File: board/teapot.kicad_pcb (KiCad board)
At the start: 2 copper layers, 49.9 x 50 mm, 47 parts, among them J1 MICROUSB, P1 BATT, P2 SMA, Q1 TEPT4400, U1 TPS79333DBVR, U2 TLV61225, U4 RFM69W, U5 STM32L052K8, U6 HTU21D, U7 MS5637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

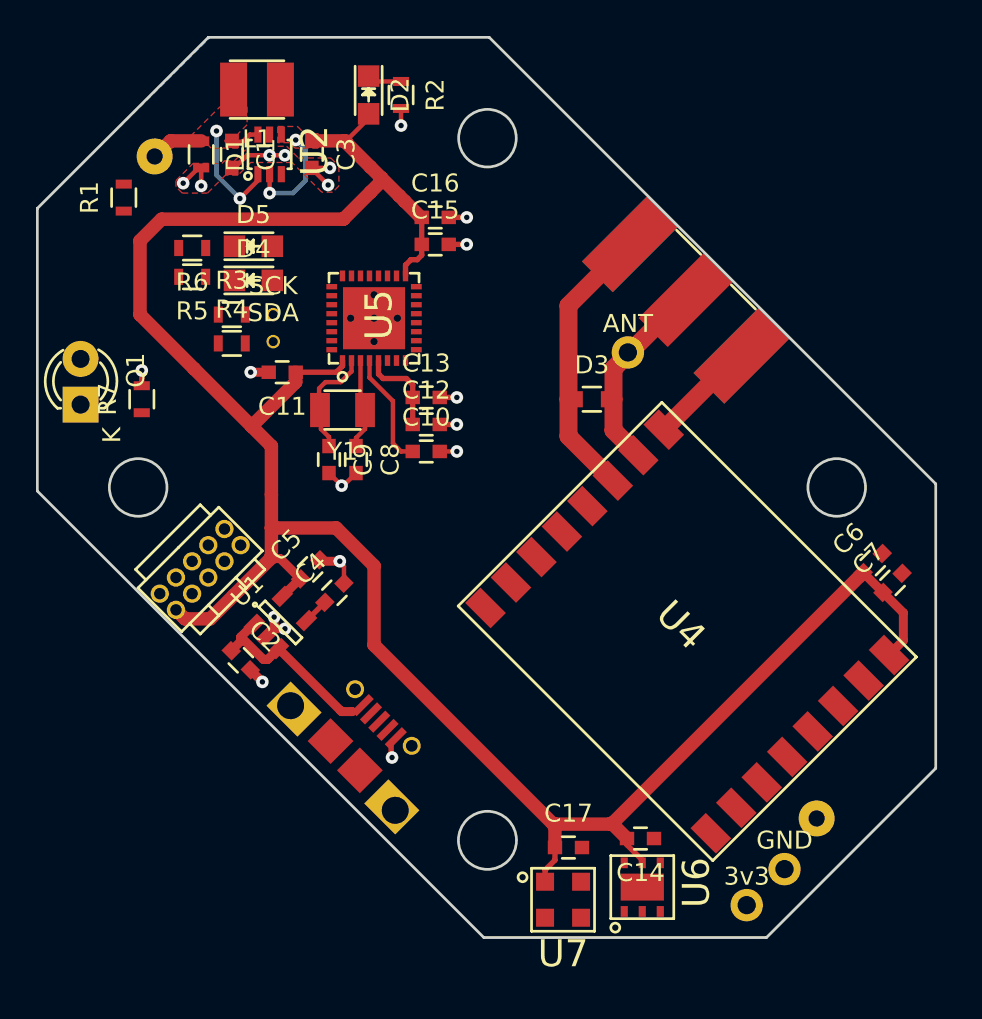
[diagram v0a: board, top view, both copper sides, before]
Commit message: Second test route on new outline/placement
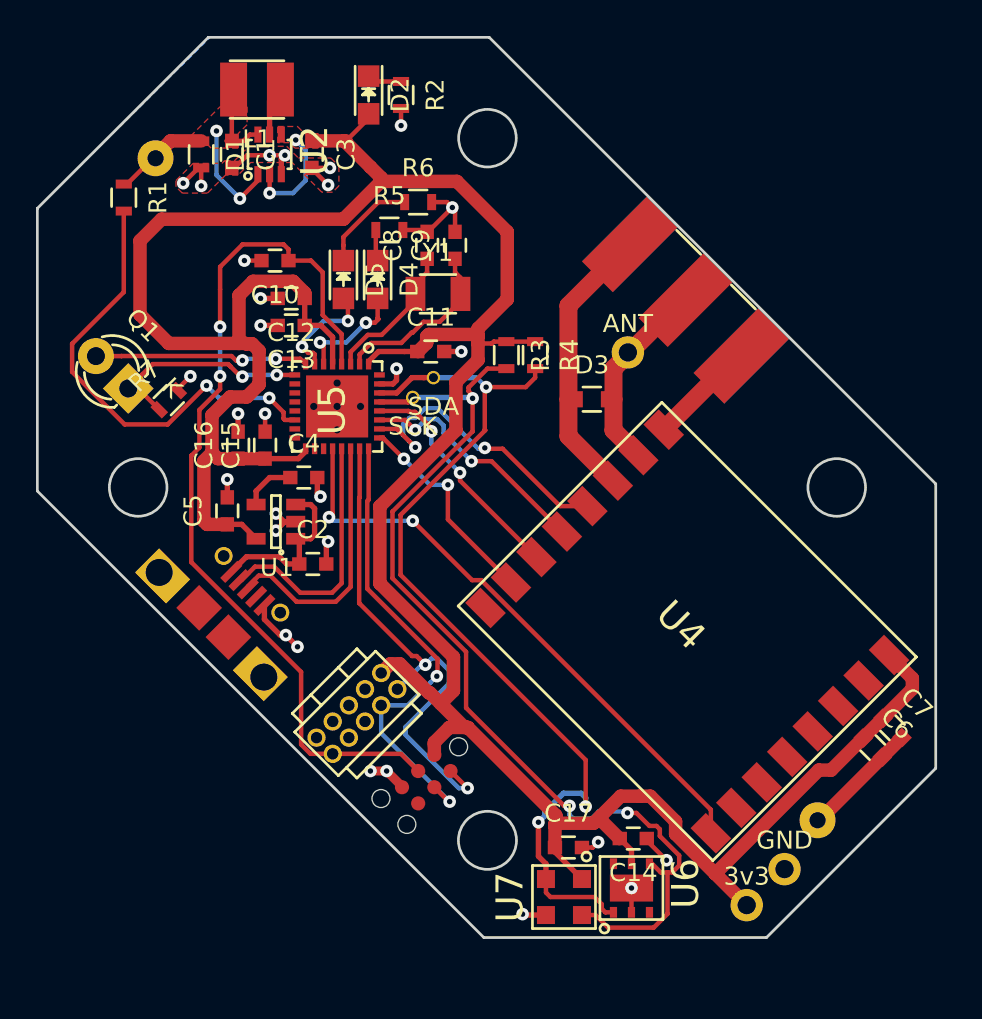
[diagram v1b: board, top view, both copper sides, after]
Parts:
- added P3: SWD_TC, agg:TC2030-NL, F.Cu at (123.6, 129.2)
- moved R4 16.9 mm to (129.7, 105.7), turned to 270 degrees
- moved C16 16.7 mm to (113.2, 110.7), turned to 90 degrees
- moved R3 15.4 mm to (128.1, 105.7), turned to 270 degrees
- moved C15 14.6 mm to (114.7, 110.7), turned to 90 degrees
- moved U8 14.2 mm to (122.0, 124.2), turned to 225 degrees
- moved C9 13.8 mm to (125.2, 99.5), turned to 90 degrees
- moved C10 13.5 mm to (115.2, 100.4), turned to 180 degrees
- moved R6 12.8 mm to (123.2, 97.2), turned to 0 degrees
- moved C8 12.5 mm to (123.7, 99.5), turned to 90 degrees
- moved R5 11.3 mm to (121.5, 98.7), turned to 0 degrees
- moved J1 10.4 mm to (111.8, 120.5)
- moved C12 10.3 mm to (116.1, 102.5), turned to 180 degrees
- moved C6 10.2 mm to (148.4, 127.5), turned to 315 degrees
- moved TP5 9.12 mm to (124.0, 106.9), turned to 180 degrees
- moved TP4 9.01 mm to (122.8, 108.0), turned to 180 degrees
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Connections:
- net /USB_DM renamed /USB_D-
- net /USB_DP renamed /USB_D+
- U5 pad 10: /RFM_NSS -> (no net)
- U5 pad 11: /RFM_SCK -> (no net)
- U5 pad 12: /RFM_MISO -> (no net)
- U5 pad 13: /RFM_MOSI -> (no net)
- U5 pad 20: /LIGHT_EN -> /RFM_RESET
- U5 pad 25: /LED_GREEN -> /RFM_NSS
- U5 pad 26: /LED_YELLOW -> /RFM_SCK
- U5 pad 27: (no net) -> /RFM_MISO
- U5 pad 28: (no net) -> /RFM_MOSI
- U5 pad 6: (no net) -> /LED_GREEN
- U5 pad 7: (no net) -> /LED_YELLOW
- U5 pad 8: /LIGHT_SENSE -> /LIGHT_EN
- U5 pad 9: /RFM_RESET -> /LIGHT_SENSE
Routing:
- net /I2C_SCK: track 0.00 -> 55.8 mm, vias 0 -> 3
- net /I2C_SDA: track 0.00 -> 52.0 mm, vias 0 -> 3
- net /nRST: track 6.42 -> 49.6 mm, vias 0 -> 2
- net +3V3: track 139.6 -> 177.4 mm
- net /RFM_RESET: track 0.00 -> 33.4 mm, vias 0 -> 2
- net /SWDIO: track 0.00 -> 28.3 mm, vias 0 -> 2
- net /SWCLK: track 0.00 -> 26.2 mm, vias 0 -> 2
- net /BATT_MON: track 0.00 -> 25.7 mm, vias 0 -> 2
- net GND: track 46.7 -> 70.7 mm, vias 20 -> 29
- net /RFM_SCK: track 0.00 -> 17.6 mm, vias 0 -> 2
- net /USB_D+: track 0.00 -> 14.7 mm
- net /USB_D-: track 0.00 -> 14.3 mm
- net /RFM_MISO: track 0.00 -> 13.5 mm, vias 0 -> 2
- net /RFM_MOSI: track 0.00 -> 13.4 mm, vias 0 -> 2
- net /RFM_NSS: track 0.00 -> 12.4 mm, vias 0 -> 2
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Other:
- net class Default: clearance 0.15 -> 0.2
- rule trace_clearance: 0.15 -> 0.2

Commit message: Rerouted most of test route 2
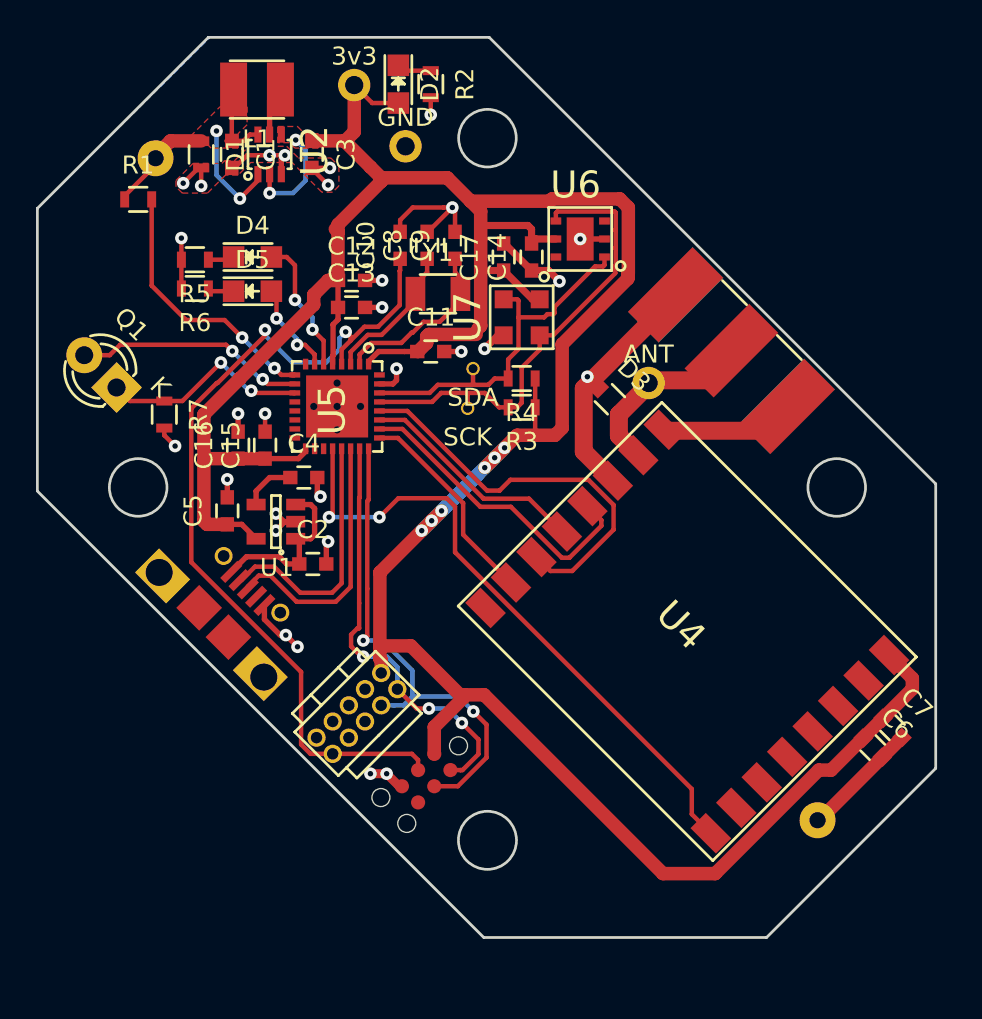
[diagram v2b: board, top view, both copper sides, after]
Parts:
- moved TP2 50.5 mm to (119.6, 90.7)
- moved TP3 45.3 mm to (122.5, 94.0)
- moved U6 36.2 mm to (132.2, 99.2), turned to 180 degrees
- moved C17 33.0 mm to (127.9, 100.2), turned to 90 degrees
- moved C14 32.8 mm to (129.4, 100.2), turned to 90 degrees
- moved U7 32.3 mm to (128.9, 103.5)
- moved R6 13.3 mm to (110.8, 102.0), turned to 180 degrees
- moved R5 10.9 mm to (110.8, 100.3), turned to 180 degrees
- moved D4 7.06 mm to (114.0, 100.2), turned to 0 degrees
- moved C10 7.00 mm to (122.2, 99.5), turned to 90 degrees
- moved D5 5.09 mm to (114.0, 102.1), turned to 0 degrees
- moved P2 3.79 mm to (140.6, 105.4)
- moved C12 3.50 mm to (119.5, 101.5), turned to 0 degrees
- moved C13 3.50 mm to (119.5, 103.0), turned to 0 degrees
- moved TP4 3.11 mm to (125.9, 108.6)
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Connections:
- U5 pad 10: (no net) -> /LIGHT_EN
- U5 pad 11: (no net) -> /LIGHT_SENSE
- U5 pad 14: /BATT_MON -> (no net)
- U5 pad 8: /LIGHT_EN -> (no net)
- U5 pad 9: /LIGHT_SENSE -> /BATT_MON
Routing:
- net /I2C_SDA: track 52.0 -> 20.4 mm, vias 3 -> 0
- net /I2C_SCK: track 55.8 -> 26.7 mm, vias 3 -> 0
- net /BATT_MON: track 25.7 -> 15.3 mm
- net /RFM_MOSI: track 13.4 -> 22.6 mm, vias 2 -> 0
- net /SWDIO: track 28.3 -> 24.1 mm, vias 2 -> 3
- net Net-(D5-Pad1): track 5.51 -> 1.46 mm
- net GND: track 70.7 -> 74.4 mm
- net +3V3: track 177.4 -> 180.5 mm, vias 2 -> 8
- net /RFM_RESET: track 33.4 -> 35.8 mm
- net Net-(D3-Pad2): track 13.1 -> 10.9 mm
- net /SWCLK: track 26.2 -> 27.7 mm
- net /LED_GREEN: track 6.24 -> 7.65 mm
- net /LIGHT_EN: track 12.0 -> 12.8 mm
- net /LED_YELLOW: track 6.06 -> 5.30 mm
- net /RFM_MISO: track 13.5 -> 12.7 mm, vias 2 -> 0
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
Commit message: Re-orientated RFM69W
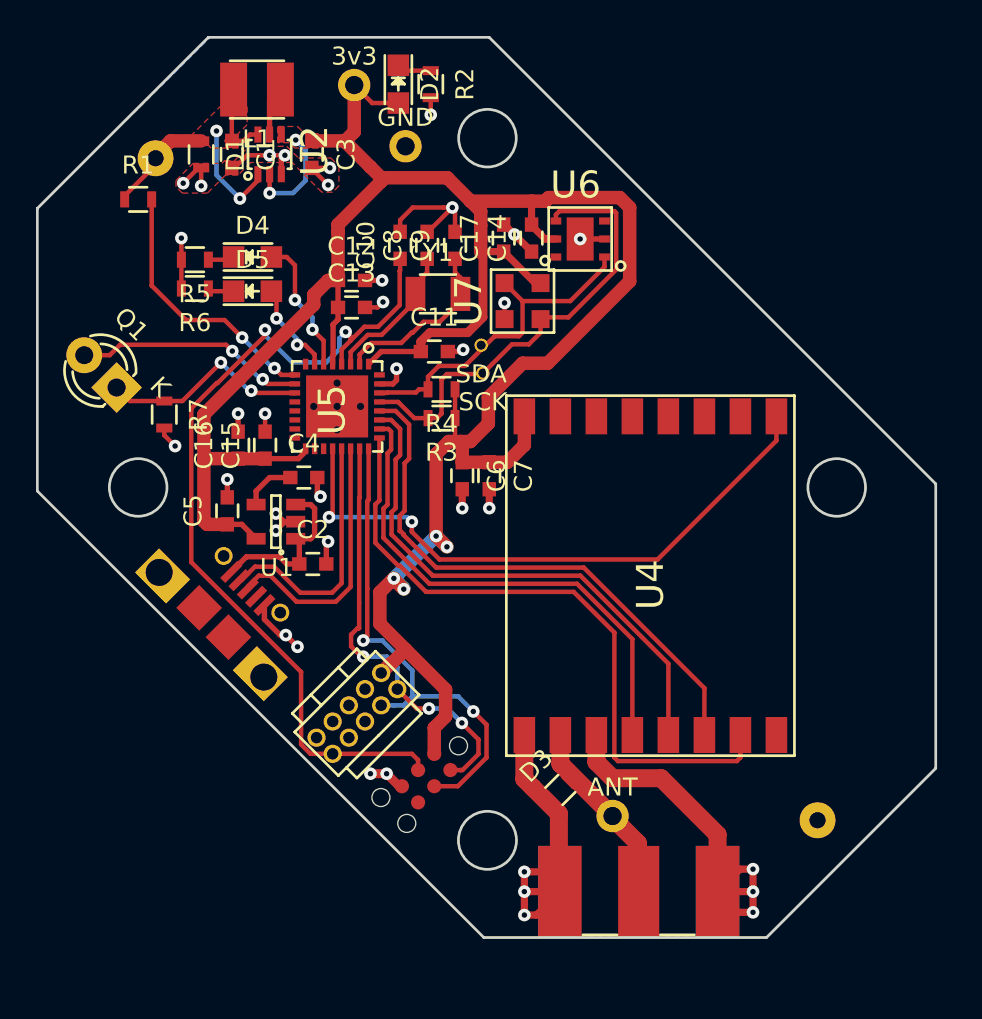
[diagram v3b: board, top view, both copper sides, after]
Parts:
- moved P2 30.5 mm to (135.4, 135.4), turned to 180 degrees
- moved C6 27.3 mm to (125.6, 112.3), turned to 270 degrees
- moved C7 26.4 mm to (127.1, 112.3), turned to 270 degrees
- moved TP1 24.1 mm to (133.9, 131.2)
- moved D3 21.9 mm to (131.1, 129.8), turned to 45 degrees
- moved R3 4.49 mm to (124.5, 109.2)
- moved R4 4.49 mm to (124.5, 107.5)
- moved U4 3.72 mm to (136.1, 117.9), turned to 270 degrees
- moved TP4 2.13 mm to (126.8, 106.7)
- moved TP5 1.38 mm to (126.7, 105.1)
- moved C14 1.05 mm to (129.4, 99.2)
- moved C17 1.05 mm to (127.9, 99.2)
- moved U7 0.90 mm to (128.9, 102.7)
- moved C11 0.20 mm to (124.0, 105.5)
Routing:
- net +3V3: track 180.5 -> 145.6 mm, vias 8 -> 6
- net /RFM_NSS: track 11.7 -> 36.6 mm
- net /RFM_MISO: track 12.7 -> 29.7 mm
- net GND: track 74.4 -> 89.1 mm, vias 29 -> 36
- net /RFM_SCK: track 17.4 -> 28.3 mm
- net /RFM_MOSI: track 22.6 -> 31.3 mm
- net /RFM_RESET: track 35.8 -> 34.1 mm
- net /I2C_SDA: track 20.4 -> 19.1 mm
- net /I2C_SCK: track 26.7 -> 25.5 mm
- net Net-(D3-Pad2): track 10.9 -> 11.8 mm

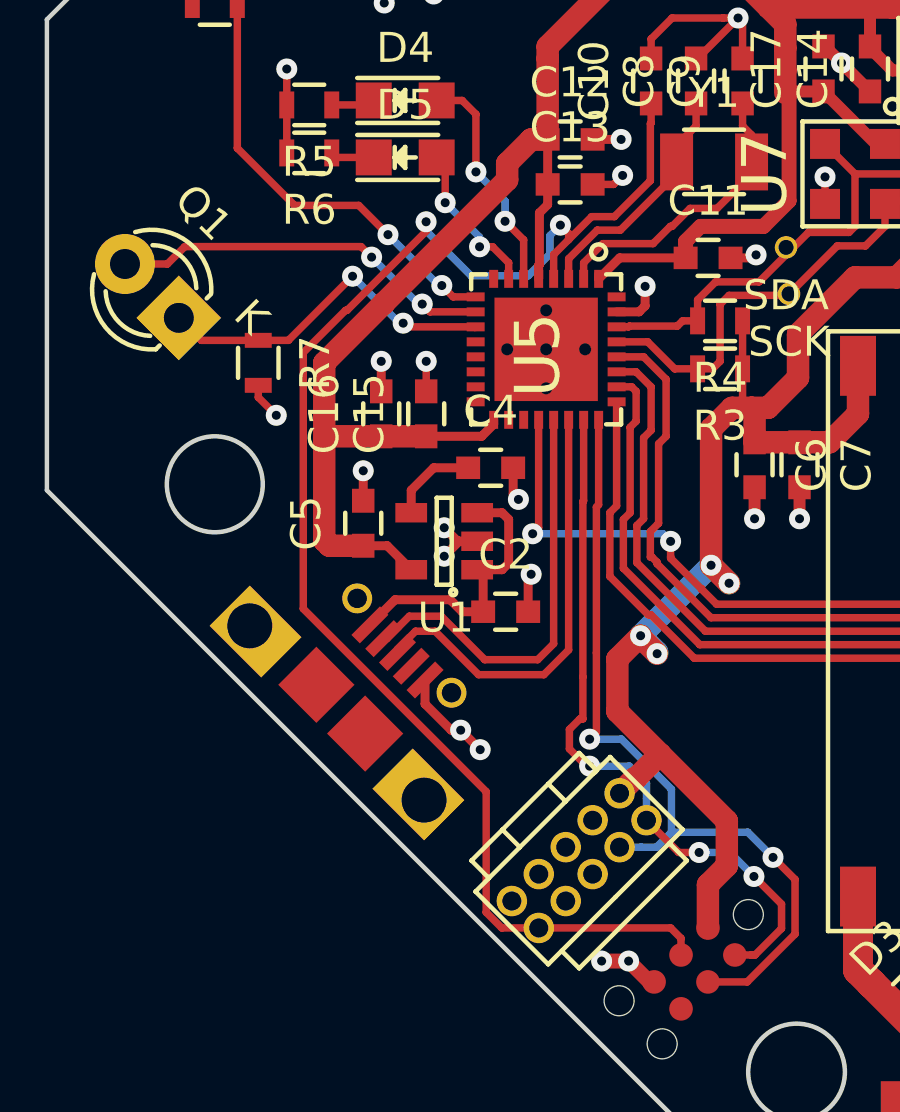
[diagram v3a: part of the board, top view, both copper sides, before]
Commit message: Updated microusb part
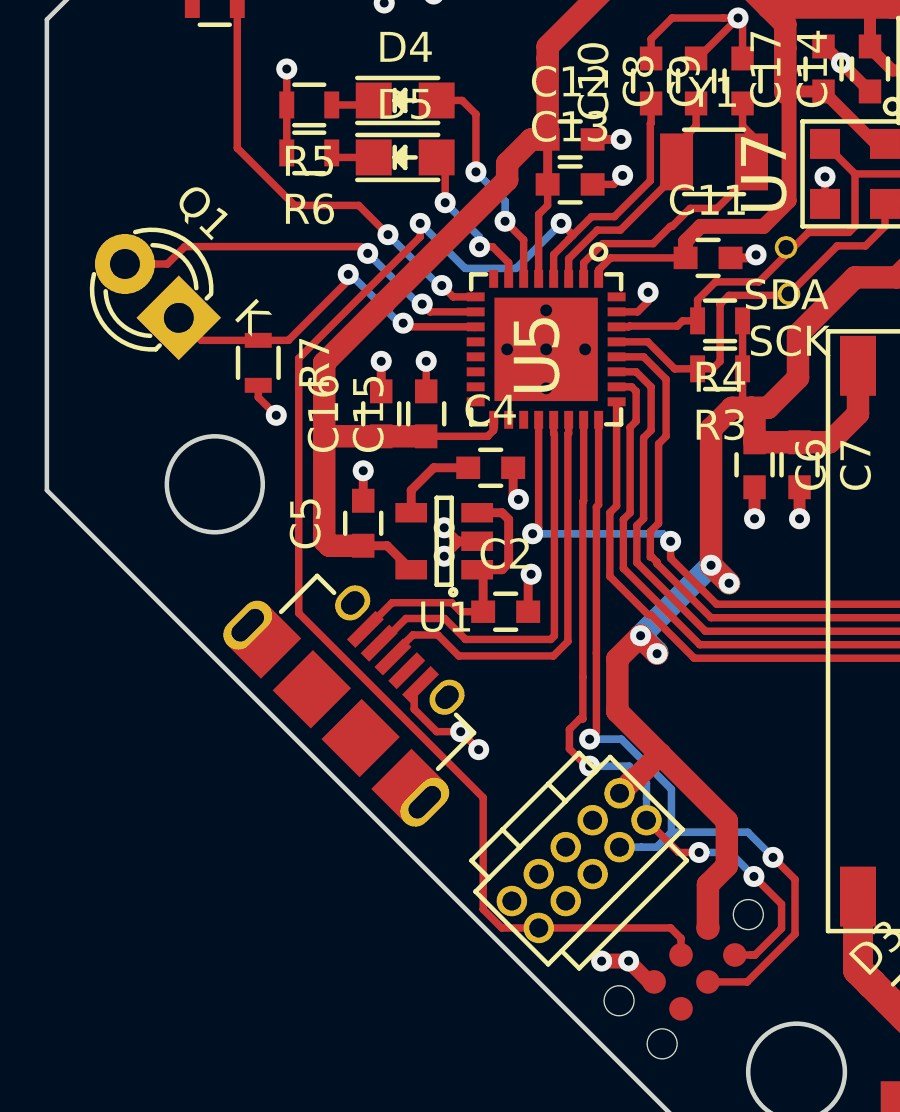
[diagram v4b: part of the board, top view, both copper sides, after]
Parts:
- moved J1 0.21 mm to (111.7, 120.7), turned to 315 degrees
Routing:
- net /USB_D+: track 14.7 -> 14.1 mm
- net /nRST: track 49.7 -> 49.1 mm
- net /USB_D-: track 14.3 -> 13.7 mm
